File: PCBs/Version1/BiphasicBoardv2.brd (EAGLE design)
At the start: 28.6 x 17.9 mm, 17 parts

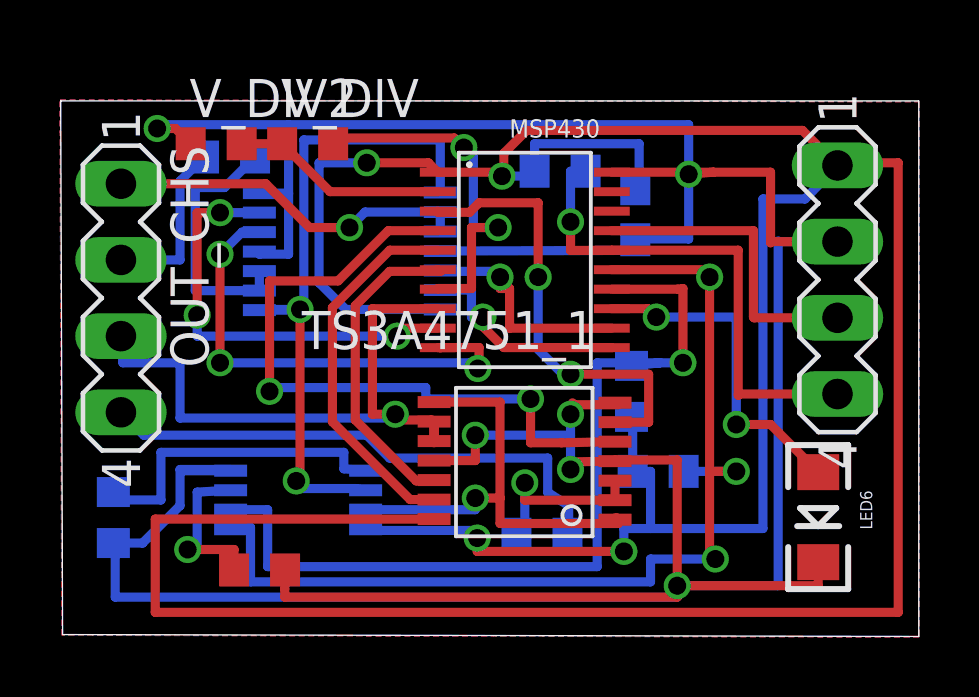
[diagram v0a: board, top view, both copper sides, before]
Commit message: Smashed a bunch of parts. Changed font sizes to 25 mil, 15% ratio
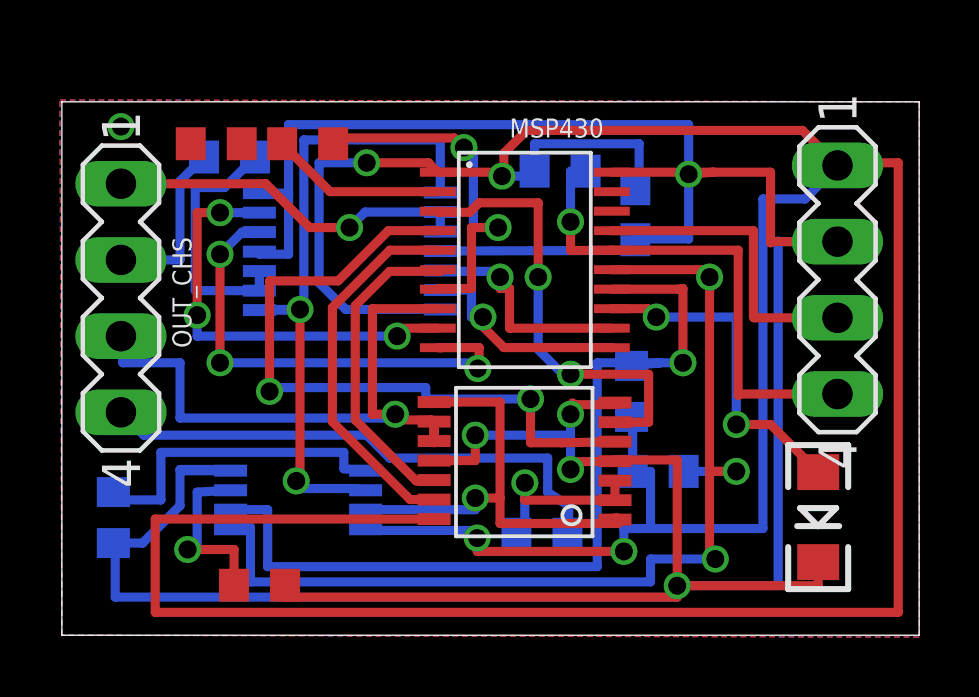
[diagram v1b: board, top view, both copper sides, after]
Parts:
- moved R_INPUT_FS1 0.51 mm to (6.59, 1.67)
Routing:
- net GND: track 131.8 -> 125.5 mm
- net N$7: track 7.20 -> 5.85 mm
- net VIA1: track 5.58 -> 6.08 mm
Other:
- board size 28.6 x 17.9 mm -> 28.6 x 17.8 mm
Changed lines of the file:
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@@
 <layer number="23" name="tOrigins" color="15" fill="1" visible="yes" active="yes"/>
 <layer number="24" name="bOrigins" color="15" fill="1" visible="yes" active="yes"/>
-<layer number="25" name="tNames" color="7" fill="1" visible="no" active="yes"/>
-<layer number="26" name="bNames" color="7" fill="1" visible="no" active="yes"/>
-<layer number="27" name="tValues" color="7" fill="1" visible="no" active="yes"/>
-<layer number="28" name="bValues" color="7" fill="1" visible="no" active="yes"/>
+<layer number="25" name="tNames" color="7" fill="1" visible="yes" active="yes"/>
+<layer number="26" name="bNames" color="7" fill="1" visible="yes" active="yes"/>
+<layer number="27" name="tValues" color="7" fill="1" visible="yes" active="yes"/>
+<layer number="28" name="bValues" color="7" fill="1" visible="yes" active="yes"/>
 <layer number="29" name="tStop" color="7" fill="3" visible="no" active="yes"/>
 <layer number="30" name="bStop" color="7" fill="6" visible="no" active="yes"/>
@@
 <board>
 <plain>
-<wire x1="0.023" y1="0.022" x2="28.562" y2="-0.0415" width="0" layer="20"/>
-<wire x1="28.562" y1="-0.0415" x2="28.562" y2="17.8095" width="0" layer="20"/>
-<wire x1="28.562" y1="17.8095" x2="-0.0405" y2="17.8095" width="0" layer="20"/>
-<wire x1="-0.0405" y1="17.8095" x2="0.023" y2="0.022" width="0" layer="20"/>
-<text x="8.546" y="1.775" size="0.6096" layer="51" font="vector" ratio="16">Biphasic v1.2</text>
+<wire x1="0" y1="0" x2="28.575" y2="0" width="0" layer="20"/>
+<wire x1="28.575" y1="0" x2="28.575" y2="17.78" width="0" layer="20"/>
+<wire x1="28.575" y1="17.78" x2="0" y2="17.78" width="0" layer="20"/>
+<wire x1="0" y1="17.78" x2="0" y2="0" width="0" layer="20"/>
+<text x="8.927" y="0.8225" size="1.016" layer="51" font="vector" ratio="15">Biphasic v1.2</text>
 </plain>
 <attributes>
@@
 <attribute name="VALUE" x="27.5035" y="11.215" size="1.27" layer="27" ratio="10" rot="R270"/>
 </element>
-<element name="R_INPUT_FS1" library="BiphasicBoard" package="R0603" value="47k" x="6.588" y="2.175" smashed="yes" rot="R180">
-<attribute name="VALUE" x="7.477" y="4.207" size="1.27" layer="27" rot="R180"/>
+<element name="R_INPUT_FS1" library="BiphasicBoard" package="R0603" value="47k" x="6.588" y="1.667" smashed="yes" rot="R180">
+<attribute name="VALUE" x="4.937" y="1.667" size="0.635" layer="27" font="vector" ratio="15" rot="R180"/>
 </element>
 <element name="R_PULLUP_SCL" library="BiphasicBoard" package="R0603" value="1k" x="18.9865" y="8.128" smashed="yes" rot="MR90">
-<attribute name="VALUE" x="16.9545" y="7.239" size="1.27" layer="28" rot="MR90"/>
+<attribute name="VALUE" x="20.1295" y="7.5565" size="0.635" layer="28" font="vector" ratio="15" rot="MR90"/>
 </element>
 <element name="R_PULLUP_SDA" library="BiphasicBoard" package="R0603" value="1k" x="19.8755" y="5.461" smashed="yes" rot="MR0">
-<attribute name="VALUE" x="21.6535" y="6.858" size="1.27" layer="28" rot="MR0"/>
+<attribute name="VALUE" x="19.558" y="4.2545" size="0.635" layer="28" font="vector" ratio="15" rot="MR180"/>
 </element>
 <element name="R_INPUT_FS0" library="BiphasicBoard" package="R0603" value="47k" x="1.715" y="3.922" smashed="yes" rot="MR90">
-<attribute name="VALUE" x="-0.317" y="3.033" size="1.27" layer="28" rot="MR90"/>
+<attribute name="VALUE" x="2.985" y="3.2235" size="0.635" layer="28" font="vector" ratio="15" rot="MR90"/>
 </element>
 <element name="R_PULLUP_RST" library="BiphasicBoard" package="R0603" value="" x="16.6065" y="15.467" smashed="yes" rot="MR0">
@@
 </element>
 <element name="DS4432U+" library="BiphasicBoard" package="8_PIN" value="" x="7.874" y="4.5085" smashed="yes" rot="MR180">
-<attribute name="NAME" x="11.8872" y="6.3627" size="0.6096" layer="26" ratio="10" rot="MR270"/>
+<attribute name="NAME" x="5.1943" y="6.9342" size="0.635" layer="26" font="vector" ratio="15" rot="MR180"/>
 </element>
 <element name="MSP430" library="BiphasicBoard" package="20_PIN" value="" x="15.4305" y="12.5095" smashed="yes" rot="R270">
-<attribute name="NAME" x="14.9186" y="16.5886" size="0.6096" layer="25"/>
-</element>
-<element name="TS3A4751_0" library="BiphasicBoard" package="14_PIN" value="" x="9.8425" y="12.0015" smashed="yes" rot="MR180">
-<attribute name="NAME" x="7.6073" y="9.9187" size="0.6096" layer="26" font="vector" ratio="10" rot="MR180"/>
-</element>
-<element name="TS3A4751_1" library="BiphasicBoard" package="14_PIN" value="" x="15.1765" y="5.0165" rot="R180"/>
-<element name="OUT_CHS" library="BiphasicBoard" package="MA04-1" value="" x="1.9685" y="11.2395" rot="R270">
+<attribute name="NAME" x="14.9186" y="16.5886" size="0.635" layer="25" font="vector" ratio="15"/>
+</element>
+<element name="TS3A4751_0" library="BiphasicBoard" package="14_PIN" value="" x="9.8425" y="12.0015" smashed="yes" rot="MR180"/>
+<element name="TS3A4751_1" library="BiphasicBoard" package="14_PIN" value="" x="15.1765" y="5.0165" smashed="yes" rot="R180">
+<attribute name="VALUE" x="18.9865" y="2.4765" size="1.27" layer="27" rot="R180"/>
+</element>
+<element name="OUT_CHS" library="BiphasicBoard" package="MA04-1" value="" x="1.9685" y="11.2395" smashed="yes" rot="R270">
 <attribute name="OC_NEWARK" value="unknown" x="1.9685" y="11.2395" size="1.778" layer="27" rot="R270" display="off"/>
 <attribute name="MPN" value="" x="1.9685" y="11.2395" size="1.778" layer="27" rot="R270" display="off"/>
 <attribute name="MF" value="" x="1.9685" y="11.2395" size="1.778" layer="27" rot="R270" display="off"/>
 <attribute name="OC_FARNELL" value="unknown" x="1.9685" y="11.2395" size="1.778" layer="27" rot="R270" display="off"/>
-</element>
-<element name="C1_SUPPLY" library="resistor" package="C0603" value="" x="19.1135" y="14.0335" rot="MR90"/>
-<element name="LED6" library="SparkFun-LED" package="LED-1206" value="GREEN" x="25.2095" y="3.937" rot="R270"/>
-<element name="R_INPUT_FS2" library="BiphasicBoard" package="R0603" value="47k" x="16.002" y="3.3655" rot="MR180"/>
-<element name="R_INPUT_FS3" library="BiphasicBoard" package="R0603" value="47k" x="5.588" y="15.9385" rot="MR180"/>
-<element name="V_DIV" library="BiphasicBoard" package="R0603" value="1M" x="8.1915" y="16.383"/>
-<element name="V_DIV2" library="BiphasicBoard" package="R0603" value="1M" x="5.1435" y="16.383"/>
+<attribute name="NAME" x="3.683" y="13.2715" size="0.635" layer="25" font="vector" ratio="15" rot="R270"/>
+<attribute name="VALUE" x="3.6195" y="10.6045" size="1.27" layer="27" ratio="10" rot="R270"/>
+</element>
+<element name="C1_SUPPLY" library="resistor" package="C0603" value="" x="19.1135" y="14.0335" smashed="yes" rot="MR90">
+<attribute name="NAME" x="20.3835" y="11.684" size="0.635" layer="26" font="vector" ratio="15" rot="MR90"/>
+<attribute name="VALUE" x="17.0815" y="13.1445" size="1.27" layer="28" rot="MR90"/>
+</element>
+<element name="LED6" library="SparkFun-LED" package="LED-1206" value="GREEN" x="25.2095" y="3.937" smashed="yes" rot="R270"/>
+<element name="R_INPUT_FS2" library="BiphasicBoard" package="R0603" value="47k" x="16.002" y="3.3655" smashed="yes" rot="MR180">
+<attribute name="VALUE" x="15.367" y="2.2225" size="0.635" layer="28" font="vector" ratio="15" rot="MR180"/>
+</element>
+<element name="R_INPUT_FS3" library="BiphasicBoard" package="R0603" value="47k" x="5.588" y="15.9385" smashed="yes" rot="MR180">
+<attribute name="VALUE" x="3.4925" y="13.7795" size="0.635" layer="28" font="vector" ratio="15" rot="MR90"/>
+</element>
+<element name="V_DIV" library="BiphasicBoard" package="R0603" value="1M" x="8.1915" y="16.383" smashed="yes">
+<attribute name="VALUE" x="9.7155" y="16.51" size="0.635" layer="27" font="vector" ratio="15"/>
+</element>
+<element name="V_DIV2" library="BiphasicBoard" package="R0603" value="1M" x="5.1435" y="16.383" smashed="yes">
+<attribute name="VALUE" x="3.7465" y="17.145" size="0.635" layer="27" font="vector" ratio="15" rot="R180"/>
+</element>
 </elements>
 <signals>
@@
 <wire x1="1.778" y1="3.1115" x2="1.715" y2="3.1115" width="0.3048" layer="16"/>
 <wire x1="1.715" y1="3.1115" x2="1.715" y2="3.072" width="0.3048" layer="16"/>
-<wire x1="7.438" y1="2.175" x2="7.4295" y2="1.54" width="0.3048" layer="1"/>
+<wire x1="7.438" y1="1.667" x2="7.4295" y2="1.54" width="0.3048" layer="1"/>
 <wire x1="20.5105" y1="1.651" x2="20.5105" y2="5.842" width="0.3048" layer="1"/>
 <wire x1="20.5105" y1="5.842" x2="18.4365" y2="5.842" width="0.3048" layer="1"/>
@@
 <wire x1="23.661" y1="13.12" x2="25.8525" y2="13.12" width="0.3048" layer="1"/>
 <contactref element="V_DIV2" pad="1"/>
-<wire x1="4.2935" y1="16.383" x2="3.7855" y2="16.891" width="0.3048" layer="1"/>
-<wire x1="3.7855" y1="16.891" x2="3.175" y2="16.891" width="0.3048" layer="1"/>
-<via x="3.175" y="16.891" extent="1-16" drill="0.6" shape="square"/>
-<wire x1="3.175" y1="16.891" x2="3.429" y2="17.018" width="0.3048" layer="16"/>
-<wire x1="3.429" y1="17.018" x2="7.5565" y2="17.018" width="0.3048" layer="16"/>
+<via x="1.9685" y="16.9545" extent="1-16" drill="0.6" shape="square"/>
 <wire x1="18.5635" y1="7.6835" x2="18.4365" y2="7.7515" width="0" layer="19" extent="1-1"/>
 </signal>
@@
 <via x="4.191" y="2.8575" extent="1-16" drill="0.6" shape="square"/>
 <wire x1="4.191" y1="2.8575" x2="5.738" y2="2.8575" width="0.3048" layer="1"/>
-<wire x1="5.738" y1="2.8575" x2="5.738" y2="2.175" width="0.3048" layer="1"/>
+<wire x1="5.738" y1="2.8575" x2="5.738" y2="1.667" width="0.3048" layer="1"/>
 </signal>
 <signal name="IN4">
@@
 <contactref element="V_DIV" pad="1"/>
 <contactref element="V_DIV2" pad="2"/>
-<wire x1="5.9935" y1="16.383" x2="7.3415" y2="16.383" width="0.3048" layer="1"/>
 <contactref element="MSP430" pad="2"/>
 <wire x1="7.3415" y1="16.383" x2="8.9401" y2="14.7844" width="0.3048" layer="1"/>
 <wire x1="8.9401" y1="14.7844" x2="12.5304" y2="14.7844" width="0.3048" layer="1"/>
+<wire x1="7.3415" y1="16.383" x2="5.9935" y2="16.383" width="0" layer="19" extent="1-1"/>
 </signal>
 </signals>

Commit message: Fixed error just introduced in CAM job. Further added values. Labels for power.
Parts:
- R_PULLUP_RST: value (none) -> R_PU_RST
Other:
- board text added: "GND"
- board text added: "VCC"
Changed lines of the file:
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@@
 <wire x1="0" y1="17.78" x2="0" y2="0" width="0" layer="20"/>
 <text x="8.927" y="0.8225" size="1.016" layer="51" font="vector" ratio="15">Biphasic v1.2</text>
+<text x="22.225" y="15.24" size="0.635" layer="51" font="vector" ratio="15">VCC</text>
+<text x="22.225" y="12.7" size="0.635" layer="51" font="vector" ratio="15">GND</text>
 </plain>
 <attributes>
@@
 </element>
 <element name="R_INPUT_FS0" library="BiphasicBoard" package="R0603" value="47k" x="1.715" y="3.922" smashed="yes" rot="MR90">
-<attribute name="VALUE" x="2.985" y="3.2235" size="0.635" layer="28" font="vector" ratio="15" rot="MR90"/>
-</element>
-<element name="R_PULLUP_RST" library="BiphasicBoard" package="R0603" value="" x="16.6065" y="15.467" smashed="yes" rot="MR0">
-<attribute name="VALUE" x="17.4955" y="13.435" size="1.27" layer="28" rot="MR0"/>
+<attribute name="VALUE" x="2.7945" y="3.287" size="0.635" layer="28" font="vector" ratio="15" rot="MR90"/>
+</element>
+<element name="R_PULLUP_RST" library="BiphasicBoard" package="R0603" value="R_PU_RST" x="16.6065" y="15.467" smashed="yes" rot="MR0">
+<attribute name="VALUE" x="18.7655" y="16.737" size="0.635" layer="28" font="vector" ratio="15" rot="MR0"/>
 </element>
 <element name="DS4432U+" library="BiphasicBoard" package="8_PIN" value="" x="7.874" y="4.5085" smashed="yes" rot="MR180">
@@
 </element>
 <element name="MSP430" library="BiphasicBoard" package="20_PIN" value="" x="15.4305" y="12.5095" smashed="yes" rot="R270">
-<attribute name="NAME" x="14.9186" y="16.5886" size="0.635" layer="25" font="vector" ratio="15"/>
+<attribute name="NAME" x="13.9661" y="16.5251" size="0.635" layer="25" font="vector" ratio="15"/>
 </element>
 <element name="TS3A4751_0" library="BiphasicBoard" package="14_PIN" value="" x="9.8425" y="12.0015" smashed="yes" rot="MR180"/>
